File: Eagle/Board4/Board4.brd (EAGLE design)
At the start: 17.8 x 25.4 mm, 39 parts, among them IC1 ESP-WROOM-02FRONT-FACE

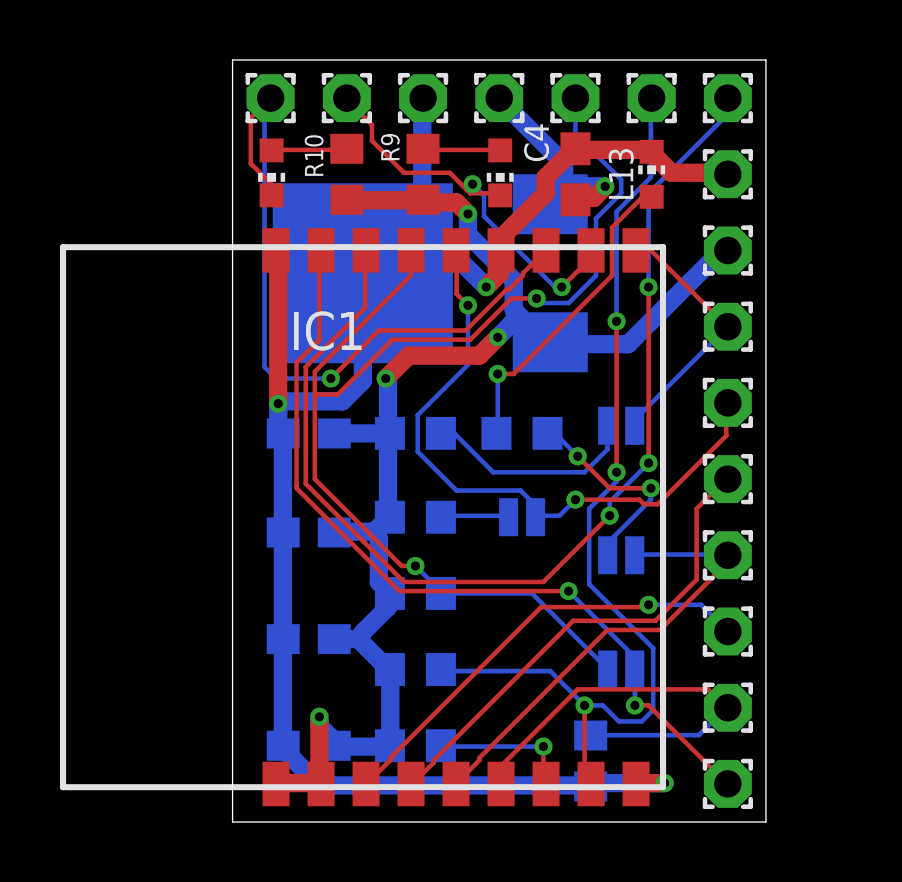
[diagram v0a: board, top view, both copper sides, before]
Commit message: 一旦没にしてましたが発売することになり復活 ・シルクを整理 ・EN端子やLEDの電流制限抵抗値を見直し
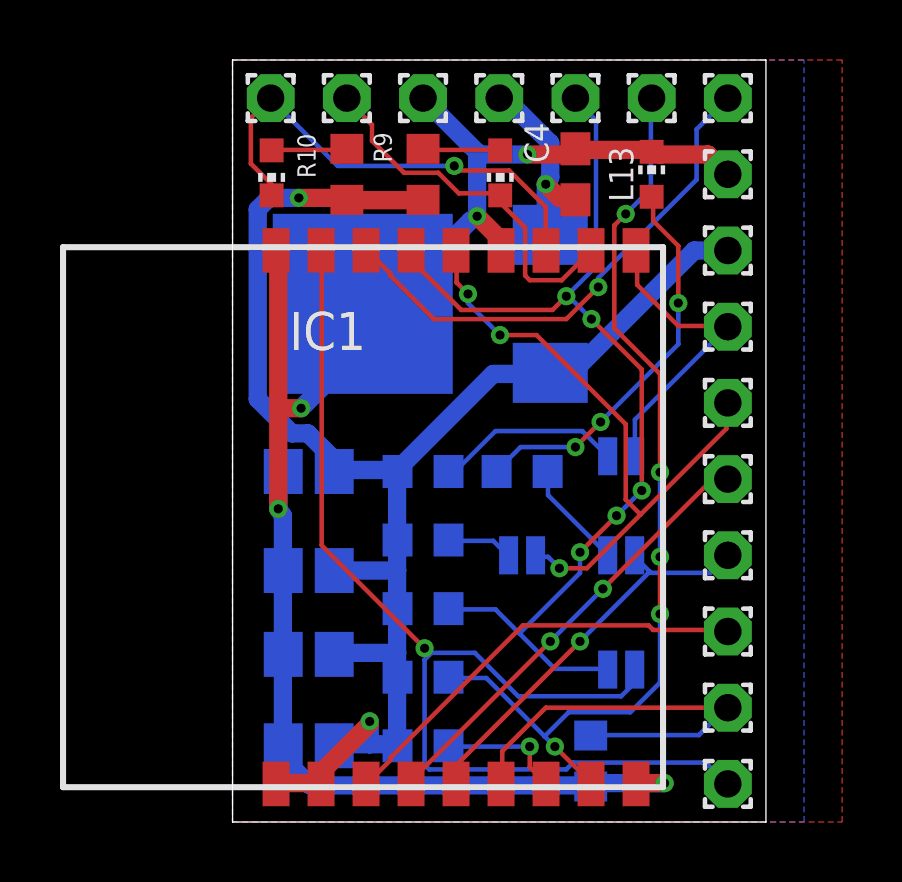
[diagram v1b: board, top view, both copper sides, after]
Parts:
- C1, C2, C3, C5: device resistor:C0603 -> resistor:C0805
- R1, R2, R4, R5, R6, R7: device _temp:R0603 -> resistor:R0603
- R10, R8, R9: value 2k2 -> 4k7; device _temp:R0603 -> resistor:R0603
- moved R5 1.30 mm to (6.35, 11.7)
- moved C3 1.27 mm to (2.54, 11.7)
- moved R8 1.27 mm to (9.65, 11.7)
- moved C5 1.27 mm to (2.54, 8.38)
- moved SJ2 1.27 mm to (9.65, 8.89)
- moved IC2 1.02 mm to (5.84, 17.3)
- moved SJ1 1.02 mm to (13.0, 12.2)
- moved R7 0.80 mm to (6.35, 9.40)
- moved R4 0.57 mm to (6.35, 7.11)
- moved C1 0.51 mm to (2.54, 5.59)
- moved R2 0.36 mm to (6.35, 4.83)
- moved R1 0.25 mm to (6.35, 2.54)
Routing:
- net N$9: track 36.6 -> 17.3 mm, vias 3 -> 1
- net N$10: track 27.7 -> 37.4 mm, vias 2 -> 1
- net N$6: track 24.2 -> 15.9 mm
- net N$8: track 39.5 -> 33.9 mm, vias 2 -> 5
- net +3V3: track 47.8 -> 52.6 mm, vias 4 -> 2
- net GND: track 61.3 -> 57.5 mm, vias 3 -> 5
- net N$17: track 7.05 -> 3.62 mm, vias 2 -> 0
- net N$18: track 10.5 -> 13.1 mm, vias 1 -> 3
- net N$16: track 15.5 -> 13.4 mm, vias 0 -> 1
- net N$4: track 8.69 -> 10.4 mm
- net N$15: track 16.2 -> 14.9 mm, vias 0 -> 2
- net N$2: track 32.8 -> 31.5 mm, vias 3 -> 5
- net N$1: track 7.83 -> 6.74 mm
- net N$11: track 7.19 -> 6.21 mm
- net N$5: track 13.6 -> 12.6 mm, vias 2 -> 0
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- added copper zone on layer 1, net GND
- added copper zone on layer 16, net GND
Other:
- board text added: "ESP-WROOM-02 / Board4 ver 1.0 by TareObjects 2016-09-16"
- board text removed: "ESP-WROOM-02 / Board4 ver 0.2 by TareObjects 2016-03-21"
